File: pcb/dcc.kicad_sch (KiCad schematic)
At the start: 46 parts, among them U12 L78L05_SOT89, U13 L79L05_SOT89, U14 LM339, U3 LM339, U4 LM339, U5 LM339, U6 LM339, U7 4052

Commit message: Finished.
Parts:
- added D10: Yellow, symbol Device:LED
- added F2: 3.15A, symbol Device:Fuse
- added F3: 100mA, symbol Device:Fuse
- added R43: 1k, symbol Device:R
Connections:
- net +5VA: now also R43.1
- net GNDA: now also D10.1 (K), F2.1, F2.2
- net K: now also F3.1, F3.2
- new net: D10.2 (A), R43.2

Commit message: Added description.
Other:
- company: (none) -> Laboratory of railway vehicles control
- title: (none) -> RailComDet - DCC part
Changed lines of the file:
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@@
 (kicad_sch (version 20230121) (generator eeschema)
   (paper "A4")
+  (title_block
+    (title "RailComDet - DCC part")
+    (company "Laboratory of railway vehicles control")
+    (comment 1 "Kateřina Hanáková")
+    (comment 2 "https://github.com/kmzbrnoI/railcomdet")
+    (comment 3 "https://creativecommons.org/licenses/by-sa/4.0/")
+    (comment 4 "Released under the Creative Commons Attribution-ShareAlike 4.0 License")
+  )
   (junction (at 60.96 69.85) (diameter 0) (color 0 0 0 0)
   )

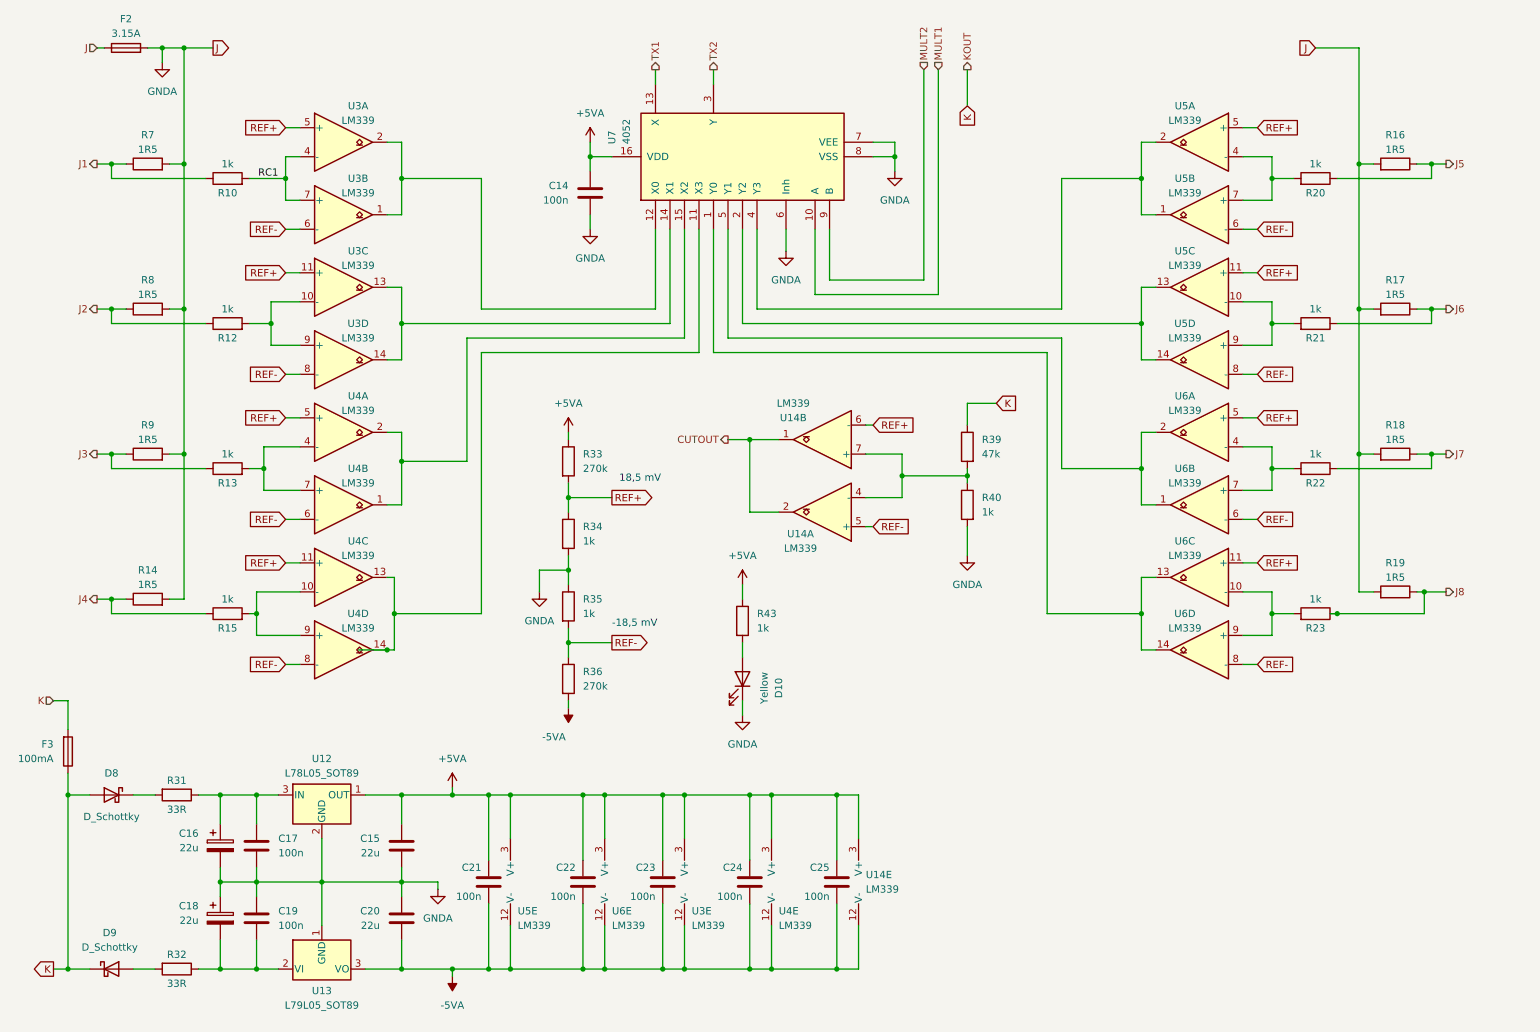
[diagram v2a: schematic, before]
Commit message: Added testpoints.
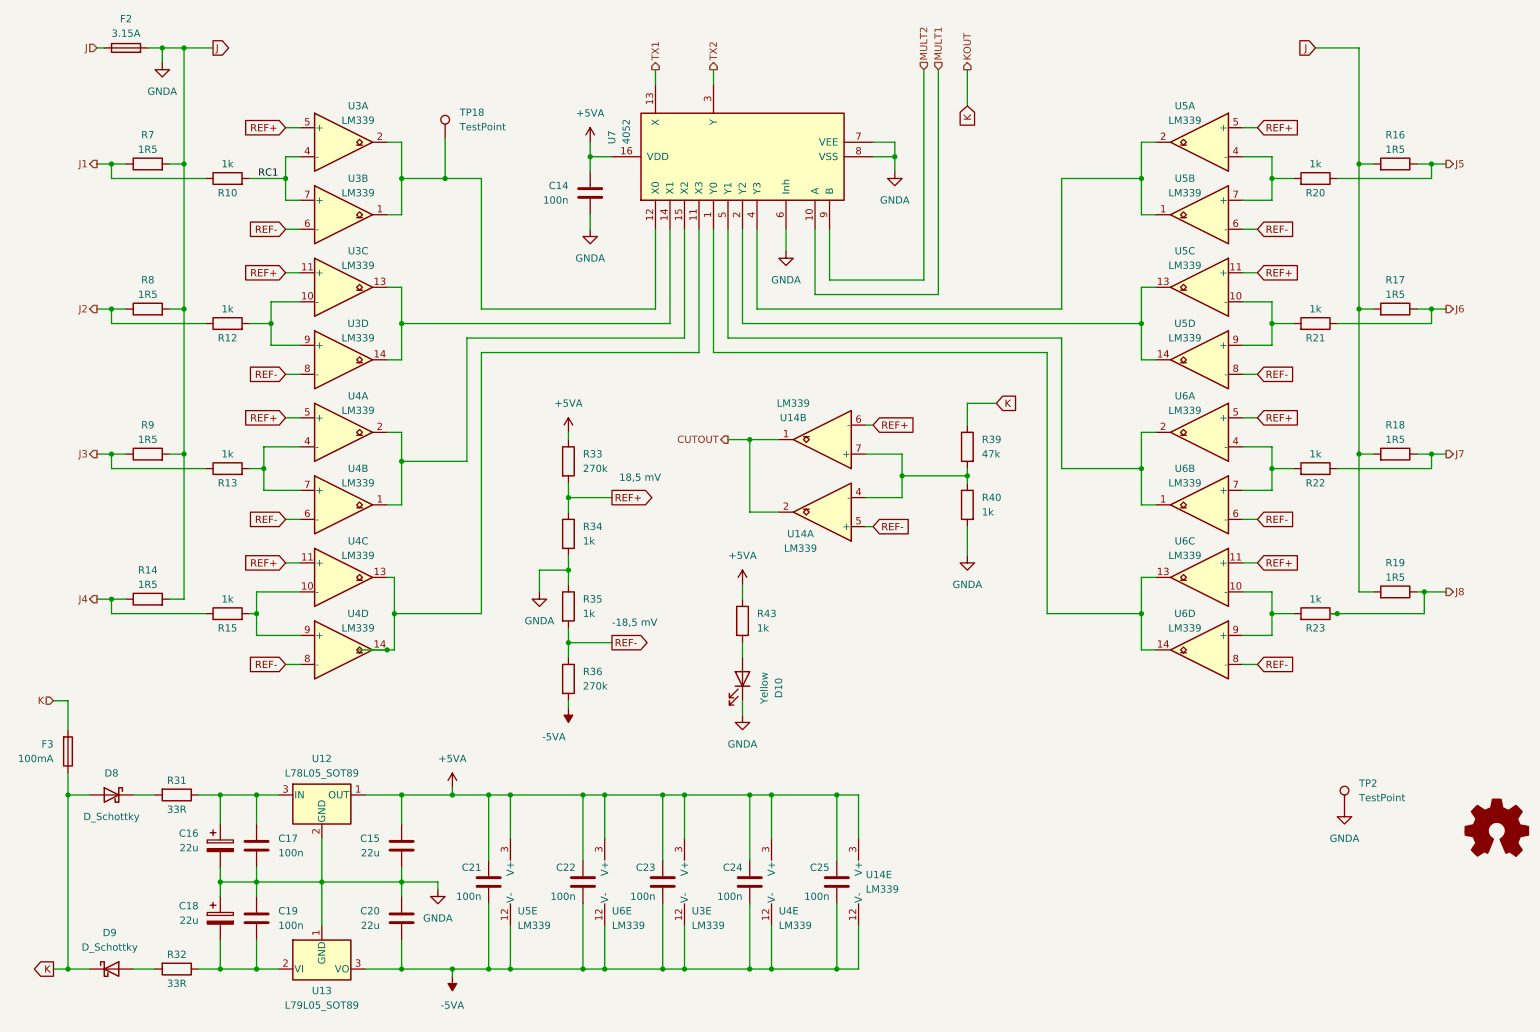
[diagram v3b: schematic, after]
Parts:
- added TP18, TP2: TestPoint, symbol Connector:TestPoint
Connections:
- net GNDA: now also TP2.1
- net at U3.1, U3.2, U7.12 (X0): now also TP18.1
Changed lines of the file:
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@@
   (junction (at 119.38 182.88) (diameter 0) (color 0 0 0 0)
   )
+  (junction (at 91.44 44.45) (diameter 0) (color 0 0 0 0)
+  )
   (junction (at 58.42 182.88) (diameter 0) (color 0 0 0 0)
   )
@@
     (stroke (width 0) (type default))
   )
-  (wire (pts (xy 83.82 44.45) (xy 97.79 44.45))
+  (wire (pts (xy 83.82 44.45) (xy 91.44 44.45))
     (stroke (width 0) (type default))
   )
@@
     (stroke (width 0) (type default))
   )
+  (wire (pts (xy 91.44 37.465) (xy 91.44 44.45))
+    (stroke (width 0) (type default))
+  )
   (wire (pts (xy 166.37 105.41) (xy 165.1 105.41))
     (stroke (width 0) (type default))
@@
   )
   (wire (pts (xy 63.5 111.76) (xy 66.04 111.76))
+    (stroke (width 0) (type default))
+  )
+  (wire (pts (xy 91.44 44.45) (xy 97.79 44.45))
     (stroke (width 0) (type default))
   )
@@
     )
   )
+  (symbol (lib_id "Graphic:Logo_Open_Hardware_Small") (at 275.59 158.75 0) (unit 1)
+    (in_bom no) (on_board no) (dnp no) (fields_autoplaced)
+    (property "Reference" "#SYM2" (at 275.59 151.765 0)
+      (effects (font (size 1.27 1.27)) hide)
+    )
+    (property "Value" "Logo_Open_Hardware_Small" (at 275.59 164.465 0)
+      (effects (font (size 1.27 1.27)) hide)
+    )
+    (property "Footprint" "" (at 275.59 158.75 0)
+      (effects (font (size 1.27 1.27)) hide)
+    )
+    (property "Datasheet" "~" (at 275.59 158.75 0)
+      (effects (font (size 1.27 1.27)) hide)
+    )
+    (property "Sim.Enable" "0" (at 275.59 158.75 0)
+      (effects (font (size 1.27 1.27)) hide)
+    )
+    (instances
+      (project "railcomdet"
+        (path "/3e59d29f-2657-4552-9290-3c54fadfdf63/c65c8567-2dc1-4e1e-ba1a-da7bb38dcfe3"
+          (reference "#SYM2") (unit 1)
+        )
+        (path "/3e59d29f-2657-4552-9290-3c54fadfdf63/e5256faa-a48e-4175-bec4-bd0fa3c5f991"
+          (reference "#SYM3") (unit 1)
+        )
+      )
+    )
+  )
   (symbol (lib_id "Comparator:LM339") (at 223.52 38.1 0) (mirror y) (unit 1)
     (in_bom yes) (on_board yes) (dnp no)
@@
     )
   )
+  (symbol (lib_id "power:GNDA") (at 248.92 154.94 0) (unit 1)
+    (in_bom yes) (on_board yes) (dnp no) (fields_autoplaced)
+    (property "Reference" "#PWR065" (at 248.92 161.29 0)
+      (effects (font (size 1.27 1.27)) hide)
+    )
+    (property "Value" "GNDA" (at 248.92 160.02 0)
+      (effects (font (size 1.27 1.27)))
+    )
+    (property "Footprint" "" (at 248.92 154.94 0)
+      (effects (font (size 1.27 1.27)) hide)
+    )
+    (property "Datasheet" "" (at 248.92 154.94 0)
+      (effects (font (size 1.27 1.27)) hide)
+    )
+    (pin "1")
+    (instances
+      (project "railcomdet"
+        (path "/3e59d29f-2657-4552-9290-3c54fadfdf63/e5256faa-a48e-4175-bec4-bd0fa3c5f991"
+          (reference "#PWR065") (unit 1)
+        )
+      )
+    )
+  )
   (symbol (lib_id "Device:R") (at 113.03 132.08 0) (unit 1)
     (in_bom yes) (on_board yes) (dnp no) (fields_autoplaced)
@@
     )
   )
+  (symbol (lib_id "Connector:TestPoint") (at 248.92 154.94 0) (unit 1)
+    (in_bom yes) (on_board yes) (dnp no) (fields_autoplaced)
+    (property "Reference" "TP2" (at 251.46 150.368 0)
+      (effects (font (size 1.27 1.27)) (justify left))
+    )
+    (property "Value" "TestPoint" (at 251.46 152.908 0)
+      (effects (font (size 1.27 1.27)) (justify left))
+    )
+    (property "Footprint" "" (at 254 154.94 0)
+      (effects (font (size 1.27 1.27)) hide)
+    )
+    (property "Datasheet" "~" (at 254 154.94 0)
+      (effects (font (size 1.27 1.27)) hide)
+    )
+    (pin "1")
+    (instances
+      (project "railcomdet"
+        (path "/3e59d29f-2657-4552-9290-3c54fadfdf63/e5256faa-a48e-4175-bec4-bd0fa3c5f991"
+          (reference "TP2") (unit 1)
+        )
+      )
+    )
+  )
   (symbol (lib_id "Device:R") (at 53.34 69.85 90) (unit 1)
     (in_bom yes) (on_board yes) (dnp no)
@@
         )
       )
+    )
+  )
+  (symbol (lib_id "Connector:TestPoint") (at 91.44 37.465 0) (unit 1)
+    (in_bom yes) (on_board yes) (dnp no) (fields_autoplaced)
+    (property "Reference" "TP18" (at 93.98 32.893 0)
+      (effects (font (size 1.27 1.27)) (justify left))
+    )
+    (property "Value" "TestPoint" (at 93.98 35.433 0)
+      (effects (font (size 1.27 1.27)) (justify left))
+    )
+    (property "Footprint" "" (at 96.52 37.465 0)
+      (effects (font (size 1.27 1.27)) hide)
+    )
+    (property "Datasheet" "~" (at 96.52 37.465 0)
+      (effects (font (size 1.27 1.27)) hide)
+    )
+    (pin "1")
+    (instances
+      (project "railcomdet"
+        (path "/3e59d29f-2657-4552-9290-3c54fadfdf63/e5256faa-a48e-4175-bec4-bd0fa3c5f991"
+          (reference "TP18") (unit 1)
+        )
+      )

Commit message: Make ERC PASS.
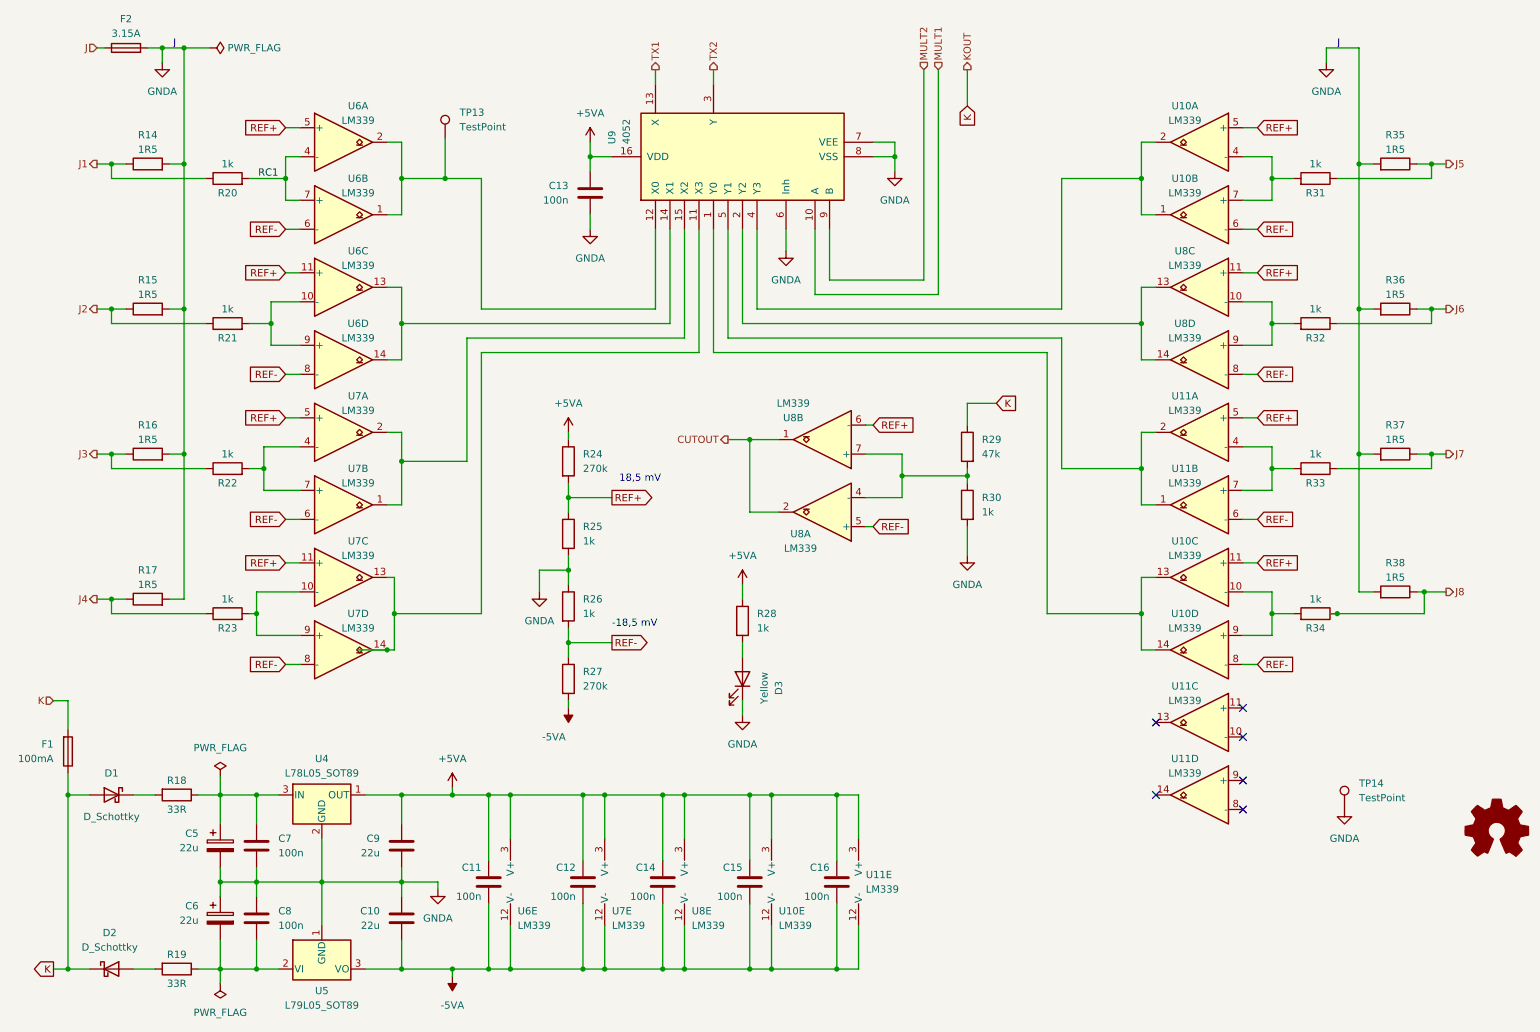
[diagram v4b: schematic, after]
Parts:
- added unit 4 of U11
- added unit 3 of U11
- renumbered C20 to C10, C21 to C11, C22 to C12, C14 to C13, C23 to C14, C24 to C15, C25 to C16, C16 to C5, C18 to C6, C17 to C7, C19 to C8, C15 to C9, D8 to D1, D9 to D2, D10 to D3, F3 to F1, R7 to R14, R8 to R15, R9 to R16, R14 to R17, R31 to R18, R32 to R19, R10 to R20, R12 to R21, R13 to R22, R15 to R23, R33 to R24, R34 to R25, R35 to R26, R36 to R27, R43 to R28, R39 to R29, R40 to R30, R20 to R31, R21 to R32, R22 to R33, R23 to R34, R16 to R35, R17 to R36, R18 to R37, R19 to R38, TP18 to TP13, TP2 to TP14, U5 to U10, U6 to U10, U4 to U10, U6 to U11, U14 to U11, U12 to U4, U13 to U5, U5 to U6, U3 to U6, U4 to U7, U6 to U7, U3 to U8, U5 to U8, U14 to U8, U7 to U9
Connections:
- net GNDA: no longer F2.1
- new net J: F2.1
- no-connect marks 0 -> 6
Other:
- note added: "J"

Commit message: Added some footprints.
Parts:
- C10, C11, C12, C13, C14, C15, C16, C5, C6, C7, C8, C9: footprint (none) -> Capacitor_SMD:C_0805_2012Metric
- D3: footprint (none) -> LED_SMD:LED_0805_2012Metric
- R20, R21, R22, R23, R28, R29, R30, R31, R32, R33, R34: footprint (none) -> Resistor_SMD:R_0805_2012Metric
- R24, R27: value 270k -> 270k/1%; footprint (none) -> Resistor_SMD:R_0805_2012Metric
- R25, R26: value 1k -> 1k/1%; footprint (none) -> Resistor_SMD:R_0805_2012Metric
- TP13, TP14: value TestPoint -> PAD; footprint (none) -> TestPoint:TestPoint_Pad_D2.0mm
- U10, U11, U6, U7, U8: footprint (none) -> Package_SO:SO-14_3.9x8.65mm_P1.27mm
- U9: footprint (none) -> Package_SO:SO-16_3.9x9.9mm_P1.27mm
